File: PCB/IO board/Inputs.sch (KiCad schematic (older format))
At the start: 69 parts

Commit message: Schematics without ESP
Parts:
- U? (x4): value MCP6004 -> MCP634
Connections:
- net +1V65 renamed +1V65_Inputs
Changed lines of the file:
@@
 LIBS:TVS_ARRAY
 LIBS:LOGIC
+LIBS:BATTERY
+LIBS:DISCRETE
+LIBS:ELECTROMECH
+LIBS:WIFI
 LIBS:Audio board-cache
 EELAYER 25 0
@@
 $Descr A4 11693 8268
 encoding utf-8
-Sheet 2 2
+Sheet 2 7
 Title ""
 Date ""
@@
 $EndComp
 Text GLabel 1350 850  2    60   Input ~ 0
-+1V65
++1V65_Inputs
 Text GLabel 1350 1250 2    60   Input ~ 0
-+1V65
-Text GLabel 1350 1550 2    60   Input ~ 0
-+1V65
++1V65_Inputs
+Text GLabel 1450 1650 3    60   Input ~ 0
++1V65_Inputs
 $Comp
 L R R?
@@
 Text GLabel 10600 2150 2    60   Output ~ 0
 ADC1-
-$Comp
-L PWR_FLAG #FLG?
-U 1 1 5AD939FB
-P 6475 2750
-F 0 "#FLG?" H 6475 2825 50  0001 C CNN
-F 1 "PWR_FLAG" H 6475 2900 50  0000 C CNN
-F 2 "" H 6475 2750 50  0001 C CNN
-F 3 "" H 6475 2750 50  0001 C CNN
-	1    6475 2750
-	1    0    0    -1
-$EndComp
-Connection ~ 6475 2850
-Wire Wire Line
-	6475 2750 6475 2850
 Connection ~ 10150 1000
 Connection ~ 10150 2150
@@
 	1825 1500 1825 1350
 Wire Wire Line
-	1275 1550 1350 1550
+	1275 1550 1450 1550
 Wire Wire Line
 	1275 1250 1350 1250
@@
 $EndComp
 Text GLabel 1350 3900 2    60   Input ~ 0
-+1V65
++1V65_Inputs
 Text GLabel 1350 4300 2    60   Input ~ 0
-+1V65
-Text GLabel 1350 4600 2    60   Input ~ 0
-+1V65
++1V65_Inputs
 $Comp
 L R R?
@@
 Text GLabel 10600 5200 2    60   Output ~ 0
 ADC2-
-$Comp
-L PWR_FLAG #FLG?
-U 1 1 5AD9B14B
-P 6475 5800
-F 0 "#FLG?" H 6475 5875 50  0001 C CNN
-F 1 "PWR_FLAG" H 6475 5950 50  0000 C CNN
-F 2 "" H 6475 5800 50  0001 C CNN
-F 3 "" H 6475 5800 50  0001 C CNN
-	1    6475 5800
-	1    0    0    -1
-$EndComp
-Connection ~ 6475 5900
-Wire Wire Line
-	6475 5800 6475 5900
 Connection ~ 10150 4050
 Connection ~ 10150 5200
@@
 	1825 4550 1825 4400
 Wire Wire Line
-	1275 4600 1350 4600
+	1275 4600 1450 4600
 Wire Wire Line
 	1275 4300 1350 4300
@@
 P 9250 2150
 F 0 "U?" H 9250 2350 50  0000 L CNN
-F 1 "MCP6004" H 9250 1950 50  0000 L CNN
+F 1 "MCP634" H 9250 1950 50  0000 L CNN
 F 2 "" H 9200 2250 50  0001 C CNN
 F 3 "" H 9300 2350 50  0001 C CNN
@@
 P 9250 4050
 F 0 "U?" H 9250 4250 50  0000 L CNN
-F 1 "MCP6004" H 9250 3850 50  0000 L CNN
+F 1 "MCP634" H 9250 3850 50  0000 L CNN
 F 2 "" H 9200 4150 50  0001 C CNN
 F 3 "" H 9300 4250 50  0001 C CNN
@@
 P 9250 5200
 F 0 "U?" H 9250 5400 50  0000 L CNN
-F 1 "MCP6004" H 9250 5000 50  0000 L CNN
+F 1 "MCP634" H 9250 5000 50  0000 L CNN
 F 2 "" H 9200 5300 50  0001 C CNN
 F 3 "" H 9300 5400 50  0001 C CNN
@@
 P 9250 1000
 F 0 "U?" H 9250 1200 50  0000 L CNN
-F 1 "MCP6004" H 9250 800 50  0000 L CNN
+F 1 "MCP634" H 9250 800 50  0000 L CNN
 F 2 "" H 9200 1100 50  0001 C CNN
 F 3 "" H 9300 1200 50  0001 C CNN
@@
 	-1   0    0    -1
 $EndComp
-Text GLabel 1300 7325 3    60   Input ~ 0
-+1V65
+Text GLabel 1400 7325 2    60   Input ~ 0
++1V65_Inputs
 Wire Wire Line
 	1300 7225 1300 7325
@@
 Text Notes 500  825  0    60   ~ 0
 Input 1
+Wire Wire Line
+	1450 1550 1450 1650
+Text GLabel 1450 4700 3    60   Input ~ 0
++1V65_Inputs
+Wire Wire Line
+	1450 4600 1450 4700
+Wire Wire Line
+	1300 7325 1400 7325
 $EndSCHEMATC

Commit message: Schematics Rev 1.0
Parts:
- gave numbers to parts that had none: 60
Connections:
- net at D201.1 (K), R212.1, U202.5 (2Y): now also U201.5 (+); no longer U201.3 (+)
- net at R209.1, RV201.3: now also U201.6 (-); no longer U201.2 (-)
- net at R209.2, R210.2: now also U201.7; no longer U201.1
- net at D203.1 (K), R226.1, U203.5 (2Y): now also U201.12 (+); no longer U201.3 (+)
- net at D203.2 (K), R215.2, R218.1: now also U201.10 (+); no longer U201.3 (+)
- net at R216.1, R219.1: now also U201.8; no longer U201.1
- net at R219.2, RV202.2: now also U201.9 (-); no longer U201.2 (-)
- net at R223.1, RV202.3: now also U201.13 (-); no longer U201.2 (-)
- net at R223.2, R224.2: now also U201.14; no longer U201.1
- no-connect marks 6 -> 8

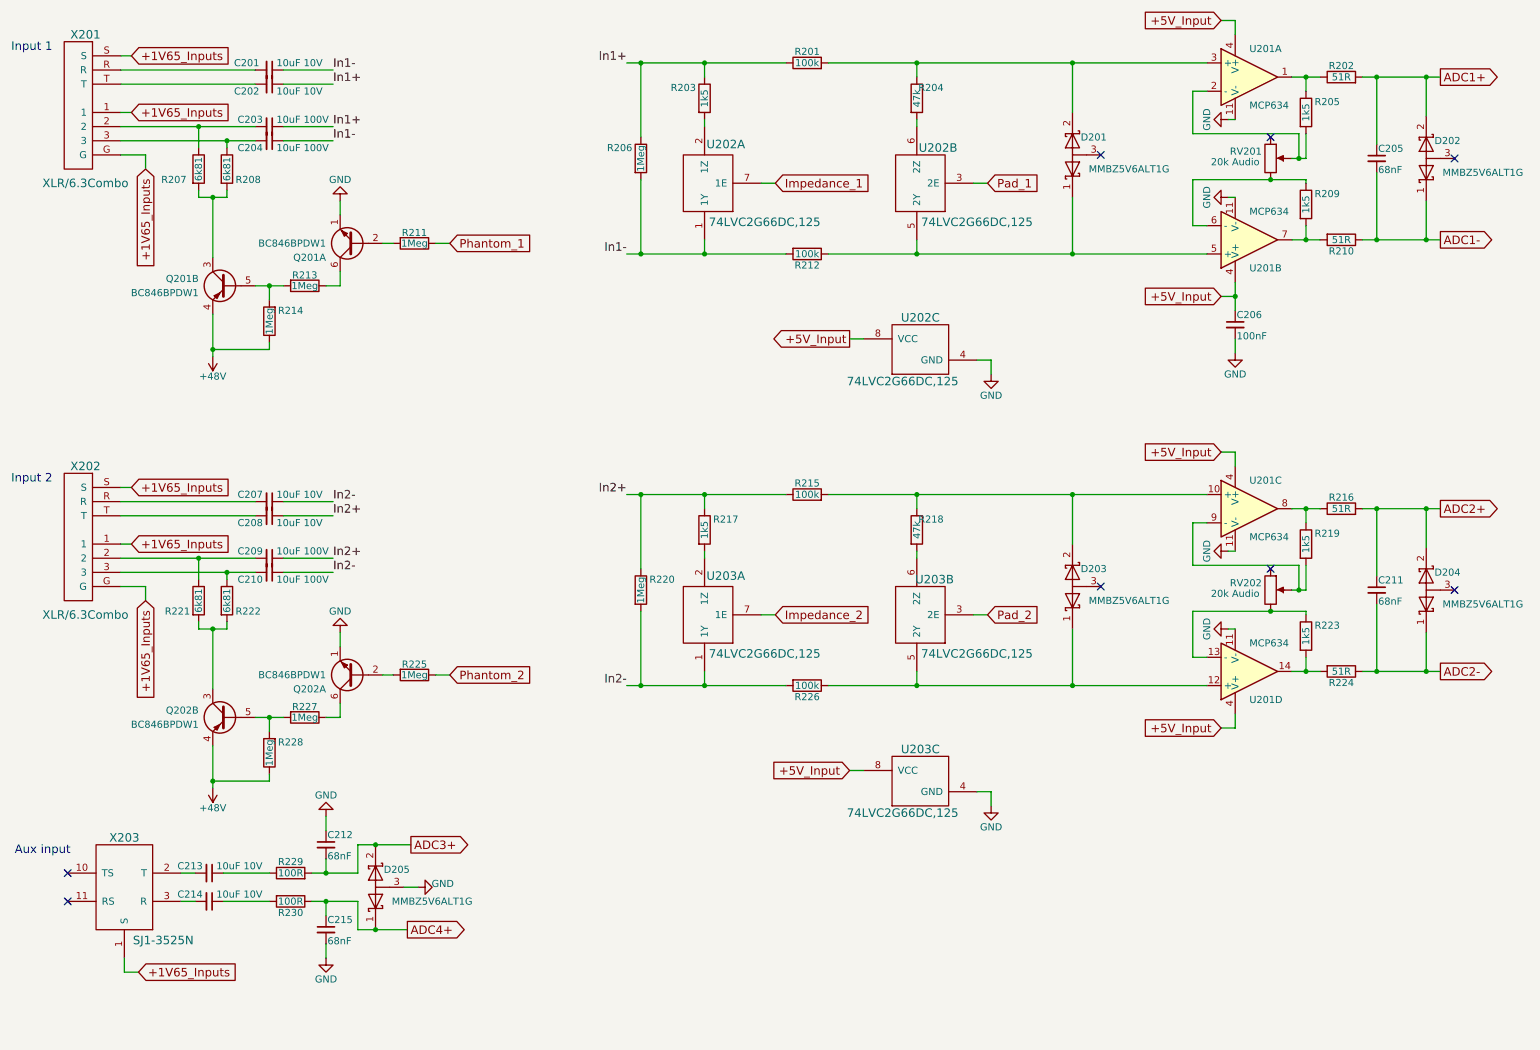
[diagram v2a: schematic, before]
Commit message: Component Placement - No pul-up
ALmost finished component placement expect for pull ups and low pass
filters for switches etc
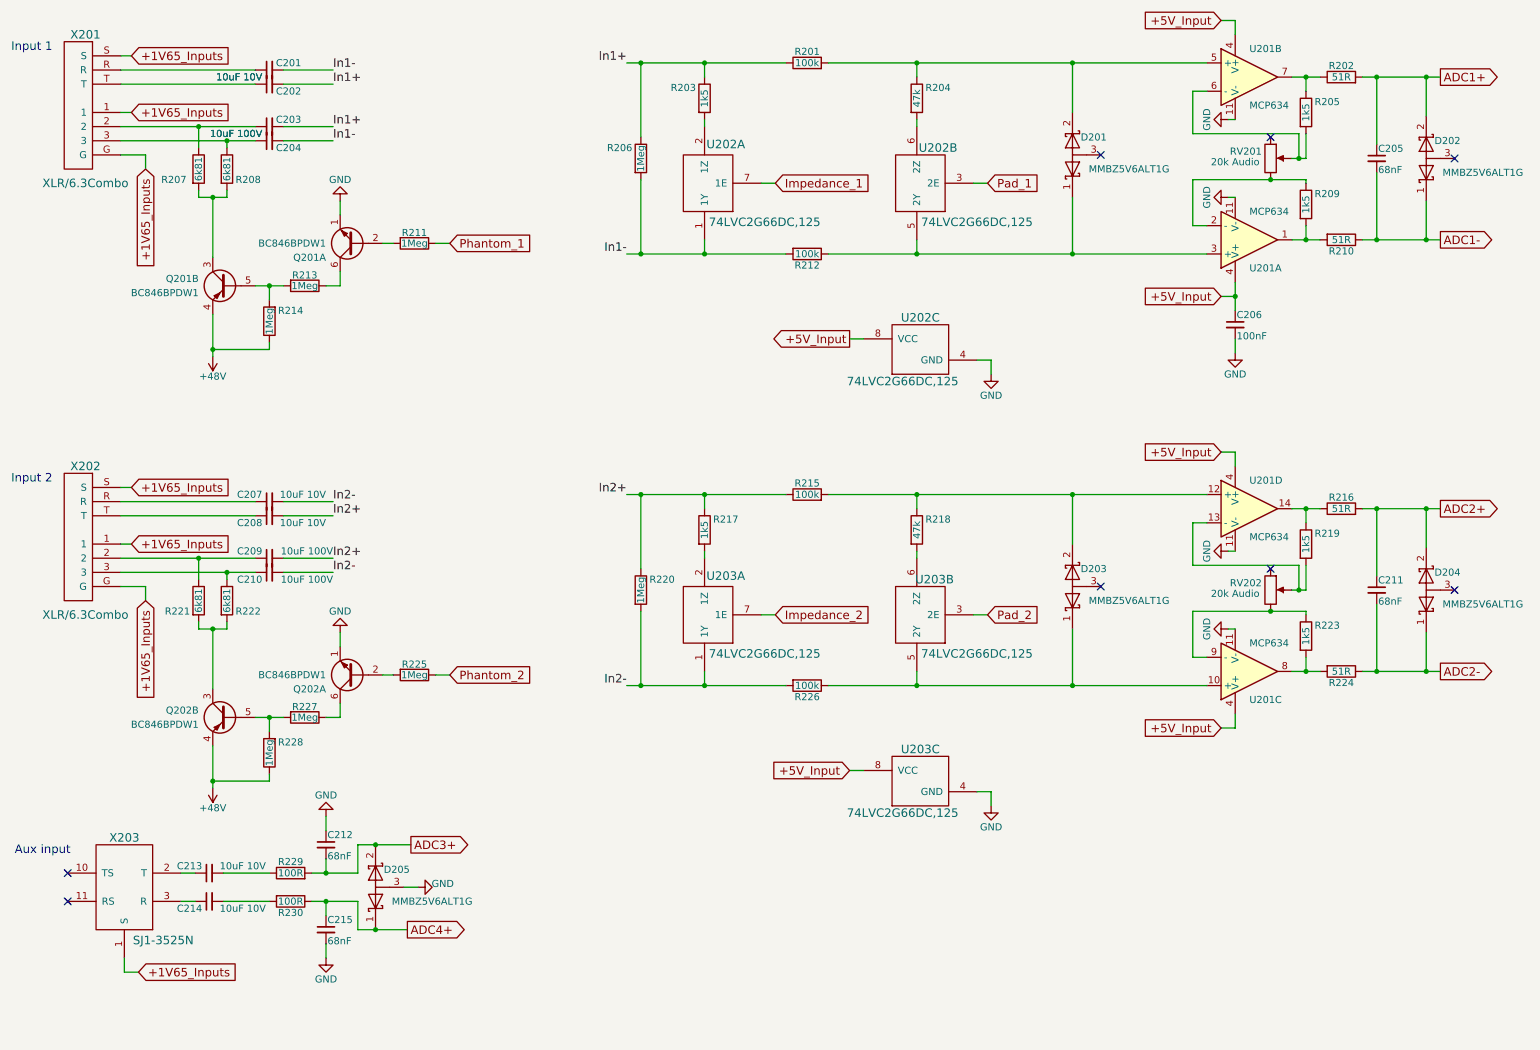
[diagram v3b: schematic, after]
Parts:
- C201, C202, C207, C208, C213, C214: footprint (none) -> Capacitors_SMD:CP_Elec_4x5.3
- C203, C204, C209, C210: footprint (none) -> Capacitors_THT:CP_Radial_D8.0mm_P3.50mm
- C205, C211, C212, C215: footprint (none) -> Capacitors_THT:C_Rect_L7.5mm_W6.5mm_P5.00mm
- C206: footprint (none) -> Capacitors_SMD:C_0603
- D201, D202, D203, D204, D205: footprint (none) -> TO_SOT_Packages_SMD:SOT-23
- Q201, Q202: footprint TO_SOT_Packages_SMD:SOT-363 -> TO_SOT_Packages_SMD:SOT-363_SC-70-6_Handsoldering
- R201, R202, R203, R204, R205, R206, R207, R208, R209, R210, R211, R212, R213, R214, R215, R216, R217, R218, R219, R220, R221, R222, R223, R224, R225, R226, R227, R228, R229, R230: footprint (none) -> Resistors_SMD:R_0603
- RV201, RV202: footprint (none) -> ELECTROMECH:P140KH1
- U201: footprint (none) -> Housings_SSOP:TSSOP-14_4.4x5mm_Pitch0.65mm
- U202, U203: footprint (none) -> Housings_SSOP:VSSOP-8_2.4x2.1mm_Pitch0.5mm
- X201, X202: footprint (none) -> Audio Connectors:NCJ6FA-H-0
- X203: footprint (none) -> Audio Connectors:SJ1-352xN
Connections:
- net In1+: now also C202.2, C203.2; no longer C202.1, C203.1
- net In1-: now also C201.2, C204.2; no longer C201.1, C204.1
- net In2+: now also C208.2, C209.2; no longer C208.1, C209.1
- net In2-: now also C207.2, C210.2; no longer C207.1, C210.1
- net at R207.1, X201.2: now also C203.1; no longer C203.2
- net at R208.1, X201.3: now also C204.1; no longer C204.2
- net at X201.R: now also C201.1; no longer C201.2
- net at X201.T: now also C202.1; no longer C202.2
- net at D201.1 (K), R212.1, U202.5 (2Y): now also U201.3 (+); no longer U201.5 (+)
- net at D201.2 (K), R201.2, R204.1: now also U201.5 (+); no longer U201.3 (+)
- net at R202.1, R205.1: now also U201.7; no longer U201.1
- net at R205.2, RV201.2: now also U201.6 (-); no longer U201.2 (-)
- net at R209.1, RV201.3: now also U201.2 (-); no longer U201.6 (-)
- net at R209.2, R210.2: now also U201.1; no longer U201.7
- net at R221.1, X202.2: now also C209.1; no longer C209.2
- net at R222.1, X202.3: now also C210.1; no longer C210.2
- net at X202.R: now also C207.1; no longer C207.2
- net at X202.T: now also C208.1; no longer C208.2
- net at D203.1 (K), R226.1, U203.5 (2Y): now also U201.10 (+); no longer U201.12 (+)
- net at D203.2 (K), R215.2, R218.1: now also U201.12 (+); no longer U201.10 (+)
- net at R216.1, R219.1: now also U201.14; no longer U201.8
- net at R219.2, RV202.2: now also U201.13 (-); no longer U201.9 (-)
- net at R223.1, RV202.3: now also U201.9 (-); no longer U201.13 (-)
- net at R223.2, R224.2: now also U201.8; no longer U201.14
- net at X203.2 (T): now also C213.1; no longer C213.2
- net at X203.3 (R): now also C214.1; no longer C214.2
- net at R229.1: now also C213.2; no longer C213.1
- net at R230.2: now also C214.2; no longer C214.1
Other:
- moved on the sheet: U201A, U201B, U201C, U201D
